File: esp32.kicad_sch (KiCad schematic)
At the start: 13 parts, among them J11 Boot, J5 USB_C_Receptacle_USB2.0_16P, J8 Reset, U2 ESP32-S3-MINI-1

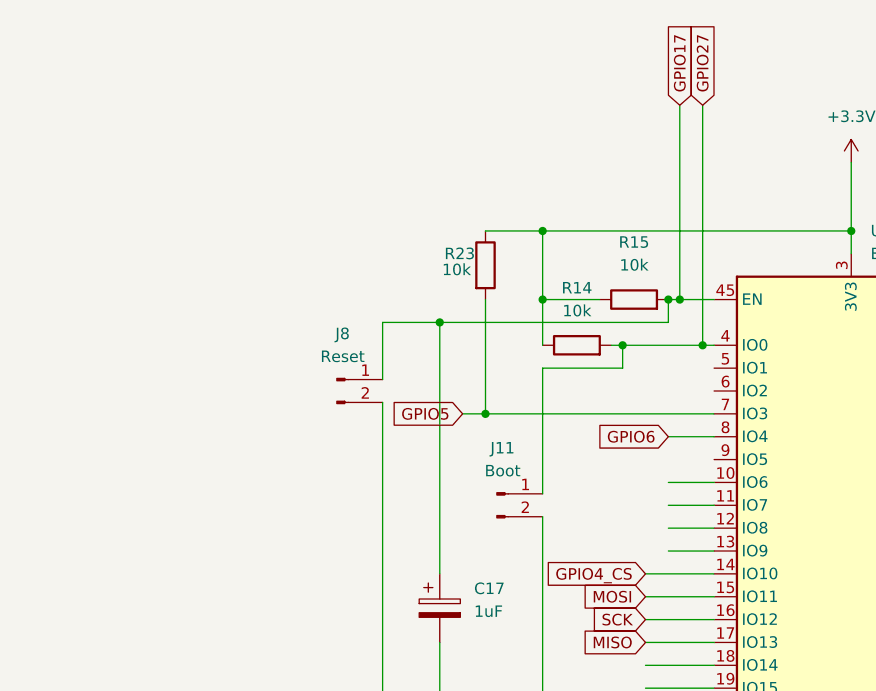
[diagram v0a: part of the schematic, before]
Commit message: Rename project to Perfect-Vision-ECU
- Rename main project files from Raspberry-Pi-Backup-power-and-GPS-hat-v4
- Update relay footprint to G6K-2F-Y to match LCSC part C397194
- Update C4 capacitor to CP_Elec_8x10.5 with LCSC C3353 (220uF 25V)
- Add new power supply schematic
- Update JLCPCB production files (gerbers, BOM, CPL)
- Remove old firmware and Raspberry Pi specific files

Co-Authored-By: Claude Opus 4.5 <noreply@anthropic.com>
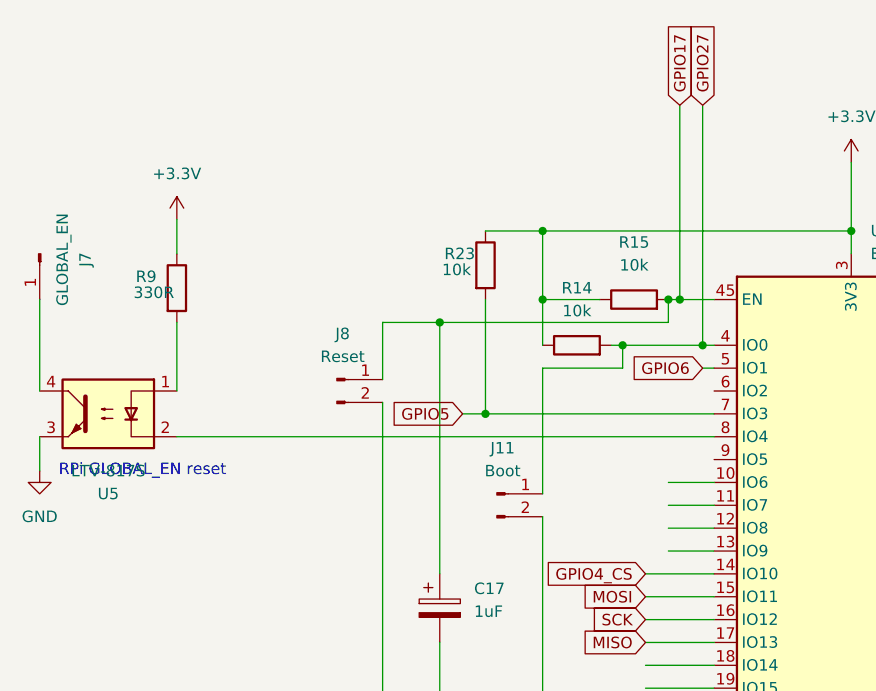
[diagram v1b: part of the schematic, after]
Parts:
- added J7: GLOBAL_EN, Connector_PinHeader_2.54mm:PinHeader_1x01_P2.54mm_Vertical, symbol Connector:Conn_01x01_Pin
- added R9: 330R, Resistor_SMD:R_0402_1005Metric, symbol Device:R
- added U5: LTV-817S, Package_DIP:SMDIP-4_W9.53mm, symbol Isolator:LTV-817S
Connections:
- net +3.3V: now also R9.1
- net GND: now also U5.3
- net GPIO6: now also U2.5 (IO1); no longer U2.8 (IO4)
- new net: R9.2, U5.1
- new net: U2.8 (IO4), U5.2
- new net: J7.1 (Pin_1), U5.4
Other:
- note added: "RPi GLOBAL_EN reset"
